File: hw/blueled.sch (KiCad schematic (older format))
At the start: 56 parts, among them J1 Barrel_Jack, J2 LED Strip, J3 ICSP, J4 Screw_Terminal_01x02, Q1 Q_PMOS_SDG, Q2 Q_PNP_EBC, SW2 PUSH, U1 ATmega328P-AU, U2 HC-05, U3 AMS1117-3.3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

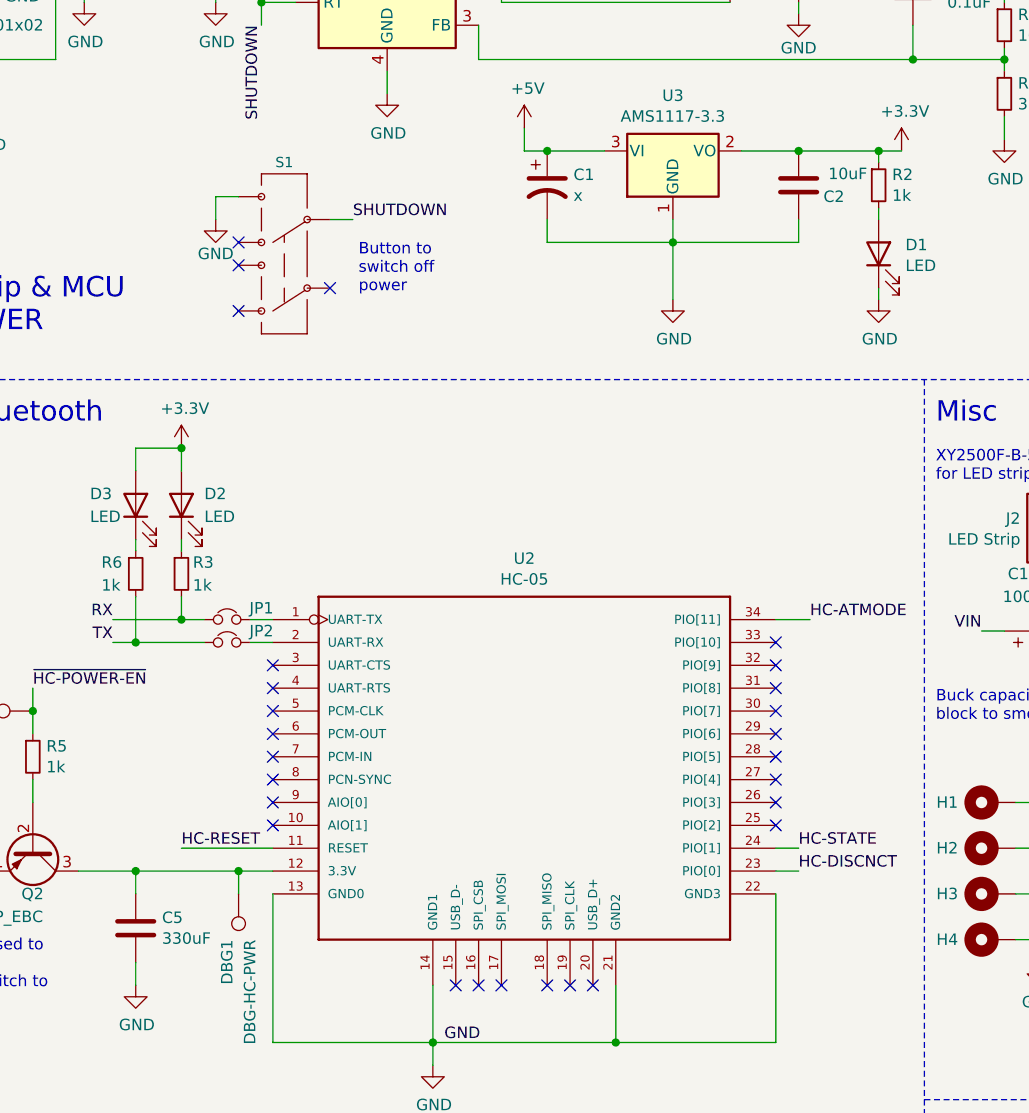
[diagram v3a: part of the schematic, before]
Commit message: add(hw): some capacitors to BOM
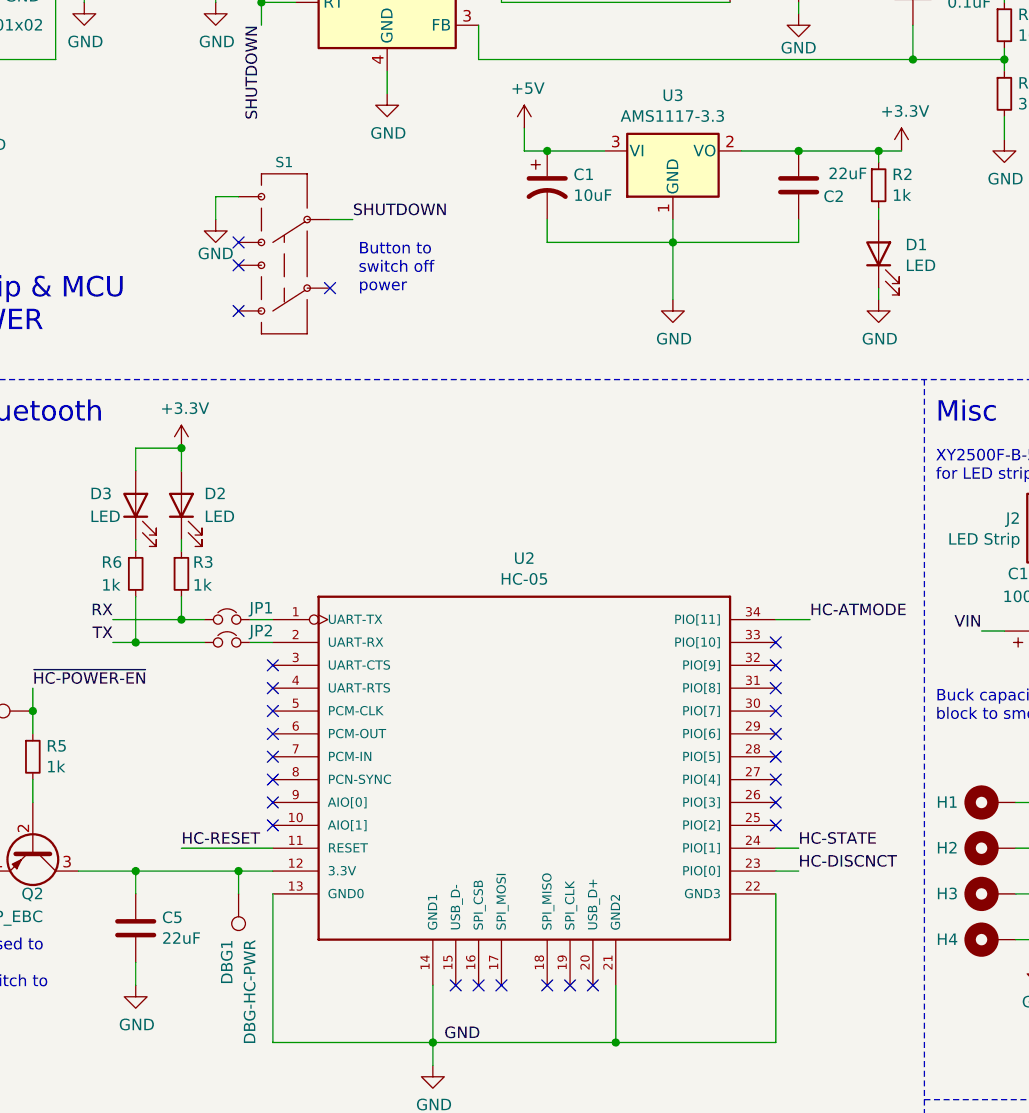
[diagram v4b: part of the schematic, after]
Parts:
- C1: value x -> 10uF
- C12: footprint Capacitor_Tantalum_SMD:CP_EIA-3216-18_Kemet-A_Pad1.58x1.35mm_HandSolder -> Capacitor_SMD:CP_Elec_10x10; Manuf. Part TAJA106K016RNJ -> VEU102M0JTR-1010
- C2: value 10uF -> 22uF; footprint Capacitor_SMD:C_0805_2012Metric_Pad1.15x1.40mm_HandSolder -> Capacitor_Tantalum_SMD:CP_EIA-3216-18_Kemet-A_Pad1.58x1.35mm_HandSolder; Manuf. Part CL21A106MQFNNNE -> 593D226X9004A2TE3
- C5: value 330uF -> 22uF; footprint (none) -> Capacitor_Tantalum_SMD:CP_EIA-3216-18_Kemet-A_Pad1.58x1.35mm_HandSolder; Distributor (none) -> lcsc.com; Manuf. Part (none) -> 593D226X9004A2TE3
- L1: footprint (none) -> blueled:SMMS1350-150M; Manuf. Part SMMS1040-150M -> MWSA1004S-150MT
- R1, R2, R3, R4, R5, R6, R7: Manuf. Part RC0805FR-071KL -> RC0805FR-071KL
- R11: Manuf. Part RK73B2ATTD102J -> RC0805FR-07470RL
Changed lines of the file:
@@
 F 3 "https://datasheet.lcsc.com/szlcsc/1810010118_YAGEO-RC0805FR-071KL_C95781.pdf" H 5100 2300 50  0001 C CNN
 F 4 "lcsc.com" H 5100 2300 50  0001 C CNN "Distributor"
-F 5 " 	RC0805FR-071KL" H 5100 2300 50  0001 C CNN "Manuf. Part"
+F 5 "RC0805FR-071KL" H 5100 2300 50  0001 C CNN "Manuf. Part"
 	1    5100 2300
 	1    0    0    -1
@@
 F 3 "https://datasheet.lcsc.com/szlcsc/1810010118_YAGEO-RC0805FR-071KL_C95781.pdf" H 7800 5050 50  0001 C CNN
 F 4 "lcsc.com" H 7800 5050 50  0001 C CNN "Distributor"
-F 5 " 	RC0805FR-071KL" H 7800 5050 50  0001 C CNN "Manuf. Part"
+F 5 "RC0805FR-071KL" H 7800 5050 50  0001 C CNN "Manuf. Part"
 	1    7800 5050
 	1    0    0    -1
@@
 F 3 "https://datasheet.lcsc.com/szlcsc/1810010118_YAGEO-RC0805FR-071KL_C95781.pdf" H 1850 4000 50  0001 C CNN
 F 4 "lcsc.com" H 1850 4000 50  0001 C CNN "Distributor"
-F 5 " 	RC0805FR-071KL" H 1850 4000 50  0001 C CNN "Manuf. Part"
+F 5 "RC0805FR-071KL" H 1850 4000 50  0001 C CNN "Manuf. Part"
 	1    1850 4000
 	1    0    0    -1
@@
 F 3 "https://datasheet.lcsc.com/szlcsc/1810010118_YAGEO-RC0805FR-071KL_C95781.pdf" H 2050 4000 50  0001 C CNN
 F 4 "lcsc.com" H 2050 4000 50  0001 C CNN "Distributor"
-F 5 " 	RC0805FR-071KL" H 2050 4000 50  0001 C CNN "Manuf. Part"
+F 5 "RC0805FR-071KL" H 2050 4000 50  0001 C CNN "Manuf. Part"
 	1    2050 4000
 	1    0    0    -1
@@
 F 3 "https://datasheet.lcsc.com/szlcsc/1810010118_YAGEO-RC0805FR-071KL_C95781.pdf" H 7700 5050 50  0001 C CNN
 F 4 "lcsc.com" H 7700 5050 50  0001 C CNN "Distributor"
-F 5 " 	RC0805FR-071KL" H 7700 5050 50  0001 C CNN "Manuf. Part"
+F 5 "RC0805FR-071KL" H 7700 5050 50  0001 C CNN "Manuf. Part"
 	1    7700 5050
 	-1   0    0    1
@@
 P 4750 2300
 F 0 "C2" H 4550 2350 50  0000 L CNN
-F 1 "10uF" H 4450 2250 50  0000 L CNN
-F 2 "Capacitor_SMD:C_0805_2012Metric_Pad1.15x1.40mm_HandSolder" H 4788 2150 50  0001 C CNN
-F 3 "https://datasheet.lcsc.com/szlcsc/1810191226_Samsung-Electro-Mechanics-CL21A106MQFNNNE_C41893.pdf" H 4750 2300 50  0001 C CNN
+F 1 "22uF" H 4450 2250 50  0000 L CNN
+F 2 "Capacitor_Tantalum_SMD:CP_EIA-3216-18_Kemet-A_Pad1.58x1.35mm_HandSolder" H 4788 2150 50  0001 C CNN
+F 3 "https://datasheet.lcsc.com/szlcsc/1809131544_Vishay-Intertech-593D226X9004A2TE3_C215881.pdf" H 4750 2300 50  0001 C CNN
 F 4 "lcsc.com" H 4750 2300 50  0001 C CNN "Distributor"
-F 5 "CL21A106MQFNNNE" H 4750 2300 50  0001 C CNN "Manuf. Part"
+F 5 "593D226X9004A2TE3" H 4750 2300 50  0001 C CNN "Manuf. Part"
 	1    4750 2300
 	-1   0    0    1
@@
 F 3 "https://datasheet.lcsc.com/szlcsc/1810010118_YAGEO-RC0805FR-071KL_C95781.pdf" H 9100 2750 50  0001 C CNN
 F 4 "lcsc.com" H 9100 2750 50  0001 C CNN "Distributor"
-F 5 " 	RC0805FR-071KL" H 9100 2750 50  0001 C CNN "Manuf. Part"
+F 5 "RC0805FR-071KL" H 9100 2750 50  0001 C CNN "Manuf. Part"
 	1    9100 2750
 	1    0    0    -1
@@
 P 3650 2300
 F 0 "C1" H 3765 2346 50  0000 L CNN
-F 1 "x" H 3765 2255 50  0000 L CNN
+F 1 "10uF" H 3765 2255 50  0000 L CNN
 F 2 "Capacitor_Tantalum_SMD:CP_EIA-3216-18_Kemet-A_Pad1.58x1.35mm_HandSolder" H 3650 2300 50  0001 C CNN
 F 3 "https://datasheet.lcsc.com/szlcsc/AVX-TAJA106K016RNJ_C7171.pdf" H 3650 2300 50  0001 C CNN
@@
 P 1850 5550
 F 0 "C5" H 1965 5596 50  0000 L CNN
-F 1 "330uF" H 1965 5505 50  0000 L CNN
-F 2 "" H 1888 5400 50  0001 C CNN
-F 3 "" H 1850 5550 50  0001 C CNN
+F 1 "22uF" H 1965 5505 50  0000 L CNN
+F 2 "Capacitor_Tantalum_SMD:CP_EIA-3216-18_Kemet-A_Pad1.58x1.35mm_HandSolder" H 1888 5400 50  0001 C CNN
+F 3 "https://datasheet.lcsc.com/szlcsc/1809131544_Vishay-Intertech-593D226X9004A2TE3_C215881.pdf" H 1850 5550 50  0001 C CNN
+F 4 "593D226X9004A2TE3" H 1850 5550 50  0001 C CNN "Manuf. Part"
+F 5 "lcsc.com" H 1850 5550 50  0001 C CNN "Distributor"
 	1    1850 5550
 	1    0    0    -1
@@
 F 3 "https://datasheet.lcsc.com/szlcsc/1810010118_YAGEO-RC0805FR-071KL_C95781.pdf" H 1400 4800 50  0001 C CNN
 F 4 "lcsc.com" H 1400 4800 50  0001 C CNN "Distributor"
-F 5 " 	RC0805FR-071KL" H 1400 4800 50  0001 C CNN "Manuf. Part"
+F 5 "RC0805FR-071KL" H 1400 4800 50  0001 C CNN "Manuf. Part"
 	1    1400 4800
 	1    0    0    -1
@@
 F 0 "L1" V 5225 1200 50  0000 C CNN
 F 1 "15uH" V 5134 1200 50  0000 C CNN
-F 2 "" H 5000 1200 50  0001 C CNN
-F 3 "https://datasheet.lcsc.com/szlcsc/1809291526_SXN-Shun-Xiang-Nuo-Elec-SMMS1040-150M_C149596.pdf" H 5000 1200 50  0001 C CNN
+F 2 "blueled:SMMS1350-150M" H 5000 1200 50  0001 C CNN
+F 3 "https://datasheet.lcsc.com/szlcsc/1912111437_Sunlord-MWSA1004S-150MT_C408488.pdf" H 5000 1200 50  0001 C CNN
 F 4 "lcsc.com" H 5000 1200 50  0001 C CNN "Distributor"
-F 5 "SMMS1040-150M" H 5000 1200 50  0001 C CNN "Manuf. Part"
+F 5 "MWSA1004S-150MT" H 5000 1200 50  0001 C CNN "Manuf. Part"
 	1    5000 1200
 	0    -1   -1   0
@@
 F 1 "470" V 8850 3800 50  0000 L CNN
 F 2 "Resistor_SMD:R_0805_2012Metric_Pad1.15x1.40mm_HandSolder" H 9050 3850 50  0001 C CNN
-F 3 "https://datasheet.lcsc.com/szlcsc/1810301711_KOA-Speer-Elec-RK73B2ATTD102J_C159911.pdf" H 9050 3850 50  0001 C CNN
+F 3 "https://datasheet.lcsc.com/szlcsc/1810311431_YAGEO-RC0805FR-07470RL_C114564.pdf" H 9050 3850 50  0001 C CNN
 F 4 "lcsc.com" H 9050 3850 50  0001 C CNN "Distributor"
-F 5 "RK73B2ATTD102J" H 9050 3850 50  0001 C CNN "Manuf. Part"
+F 5 "RC0805FR-07470RL" H 9050 3850 50  0001 C CNN "Manuf. Part"
 	1    9050 3850
 	0    -1   -1   0
@@
 F 0 "C12" V 6050 4250 50  0000 L CNN
 F 1 "1000uF" V 5950 4150 50  0000 L CNN
-F 2 "Capacitor_Tantalum_SMD:CP_EIA-3216-18_Kemet-A_Pad1.58x1.35mm_HandSolder" H 5800 4250 50  0001 C CNN
-F 3 "https://datasheet.lcsc.com/szlcsc/AVX-TAJA106K016RNJ_C7171.pdf" H 5800 4250 50  0001 C CNN
+F 2 "Capacitor_SMD:CP_Elec_10x10" H 5800 4250 50  0001 C CNN
+F 3 "https://datasheet.lcsc.com/szlcsc/1912111437_Lelon-VEU102M0JTR-1010_C249735.pdf" H 5800 4250 50  0001 C CNN
 F 4 "lcsc.com" H 5800 4250 50  0001 C CNN "Distributor"
-F 5 "TAJA106K016RNJ" H 5800 4250 50  0001 C CNN "Manuf. Part"
+F 5 "VEU102M0JTR-1010" H 5800 4250 50  0001 C CNN "Manuf. Part"
 	1    5800 4250
 	0    -1   -1   0

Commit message: add(hw): almost done with assigning capacitors
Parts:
- C10: footprint (none) -> Capacitor_SMD:C_1206_3216Metric_Pad1.42x1.75mm_HandSolder; Manuf. Part (none) -> GRM31CR60J107ME39L
- C11: footprint Capacitor_SMD:C_0603_1608Metric_Pad1.05x0.95mm_HandSolder -> Capacitor_SMD:C_0805_2012Metric_Pad1.15x1.40mm_HandSolder; Manuf. Part CC0402KRX7R0BB102 -> C2012X7R2A102KT020S
- C6: footprint Capacitor_SMD:C_1210_3225Metric_Pad1.42x2.65mm_HandSolder -> Capacitor_SMD:C_1206_3216Metric_Pad1.42x1.75mm_HandSolder; Manuf. Part C3225X7S2A475KT000N -> CGA5L3X7S2A225KT0Y0N
- C7: Manuf. Part CC0805KKX7R9BB684 -> C2012X7S2A684KT000N
- C8: footprint (none) -> Capacitor_SMD:C_0805_2012Metric_Pad1.15x1.40mm_HandSolder; Manuf. Part (none) -> C2012X7R1C474KT000N
- C9: footprint (none) -> Capacitor_SMD:C_0805_2012Metric_Pad1.15x1.40mm_HandSolder; Manuf. Part (none) -> C2012C0G1H472JT0H0N
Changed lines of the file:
@@
 F 0 "C9" H 5400 1500 50  0000 L CNN
 F 1 "0.1uF" H 5400 1400 50  0000 L CNN
-F 2 "" H 5288 1300 50  0001 C CNN
-F 3 "" H 5250 1450 50  0001 C CNN
+F 2 "Capacitor_SMD:C_0805_2012Metric_Pad1.15x1.40mm_HandSolder" H 5288 1300 50  0001 C CNN
+F 3 "https://datasheet.lcsc.com/szlcsc/1912111437_TDK-C2012C0G1H472JT0H0N_C342964.pdf" H 5250 1450 50  0001 C CNN
 F 4 "lcsc.com" H 5250 1450 50  0001 C CNN "Distributor"
-F 5 "" H 5250 1450 50  0001 C CNN "Manuf. Part"
+F 5 "C2012C0G1H472JT0H0N" H 5250 1450 50  0001 C CNN "Manuf. Part"
 	1    5250 1450
 	1    0    0    -1
@@
 F 0 "C10" H 6115 1771 50  0000 L CNN
 F 1 "100uF" H 6115 1680 50  0000 L CNN
-F 2 "" H 6000 1725 50  0001 C CNN
-F 3 "" H 6000 1725 50  0001 C CNN
+F 2 "Capacitor_SMD:C_1206_3216Metric_Pad1.42x1.75mm_HandSolder" H 6000 1725 50  0001 C CNN
+F 3 "https://datasheet.lcsc.com/szlcsc/1810201321_Murata-Electronics-GRM31CR60J107ME39L_C77085.pdf" H 6000 1725 50  0001 C CNN
 F 4 "lcsc.com" H 6000 1725 50  0001 C CNN "Distributor"
-F 5 "" H 6000 1725 50  0001 C CNN "Manuf. Part"
+F 5 "GRM31CR60J107ME39L" H 6000 1725 50  0001 C CNN "Manuf. Part"
 	1    6000 1725
 	1    0    0    -1
@@
 F 0 "C6" H 1725 1300 50  0000 L CNN
 F 1 "4.7uF" H 1675 1150 50  0000 L CNN
-F 2 "Capacitor_SMD:C_1210_3225Metric_Pad1.42x2.65mm_HandSolder" H 1625 1250 50  0001 C CNN
-F 3 "https://datasheet.lcsc.com/szlcsc/1912111437_TDK-C3225X7S2A475KT000N_C342614.pdf" H 1625 1250 50  0001 C CNN
+F 2 "Capacitor_SMD:C_1206_3216Metric_Pad1.42x1.75mm_HandSolder" H 1625 1250 50  0001 C CNN
+F 3 "https://datasheet.lcsc.com/szlcsc/1912111437_TDK-CGA5L3X7S2A225KT0Y0N_C342669.pdf" H 1625 1250 50  0001 C CNN
 F 4 "lcsc.com" H 1625 1250 50  0001 C CNN "Distributor"
-F 5 "C3225X7S2A475KT000N" H 1625 1250 50  0001 C CNN "Manuf. Part"
+F 5 "CGA5L3X7S2A225KT0Y0N" H 1625 1250 50  0001 C CNN "Manuf. Part"
 	1    1625 1250
 	1    0    0    -1
@@
 F 0 "C11" H 3350 1050 50  0000 L CNN
 F 1 "1nF" H 3350 1150 50  0000 L CNN
-F 2 "Capacitor_SMD:C_0603_1608Metric_Pad1.05x0.95mm_HandSolder" H 3638 900 50  0001 C CNN
-F 3 "https://datasheet.lcsc.com/szlcsc/2005222139_YAGEO-CC0402KRX7R0BB102_C527013.pdf" H 3600 1050 50  0001 C CNN
+F 2 "Capacitor_SMD:C_0805_2012Metric_Pad1.15x1.40mm_HandSolder" H 3638 900 50  0001 C CNN
+F 3 "https://datasheet.lcsc.com/szlcsc/1912111437_TDK-C2012X7R2A102KT020S_C415298.pdf" H 3600 1050 50  0001 C CNN
 F 4 "lcsc.com" H 3600 1050 50  0001 C CNN "Distributor"
-F 5 "CC0402KRX7R0BB102" H 3600 1050 50  0001 C CNN "Manuf. Part"
+F 5 "C2012X7R2A102KT020S" H 3600 1050 50  0001 C CNN "Manuf. Part"
 	1    3600 1050
 	0    1    1    0
@@
 F 0 "C8" H 3325 1050 50  0000 L CNN
 F 1 "0.47uF" H 3475 1050 50  0000 L CNN
-F 2 "" H 3450 850 50  0001 C CNN
-F 3 "" H 3450 850 50  0001 C CNN
+F 2 "Capacitor_SMD:C_0805_2012Metric_Pad1.15x1.40mm_HandSolder" H 3450 850 50  0001 C CNN
+F 3 "https://datasheet.lcsc.com/szlcsc/2009111606_TDK-C2012X7R1C474KT000N_C694187.pdf" H 3450 850 50  0001 C CNN
 F 4 "lcsc.com" H 3450 850 50  0001 C CNN "Distributor"
-F 5 "" H 3450 850 50  0001 C CNN "Manuf. Part"
+F 5 "C2012X7R1C474KT000N" H 3450 850 50  0001 C CNN "Manuf. Part"
 	1    3450 850
 	1    0    0    -1
@@
 F 1 "680nF" H 1950 1150 50  0000 L CNN
 F 2 "Capacitor_SMD:C_0805_2012Metric_Pad1.15x1.40mm_HandSolder" H 2238 1100 50  0001 C CNN
-F 3 "https://datasheet.lcsc.com/szlcsc/1810311413_YAGEO-CC0805KKX7R9BB684_C107133.pdf" H 2200 1250 50  0001 C CNN
+F 3 "https://datasheet.lcsc.com/szlcsc/2004221632_TDK-C2012X7S2A684KT000N_C516764.pdf" H 2200 1250 50  0001 C CNN
 F 4 "lcsc.com" H 2200 1250 50  0001 C CNN "Distributor"
-F 5 "CC0805KKX7R9BB684" H 2200 1250 50  0001 C CNN "Manuf. Part"
+F 5 "C2012X7S2A684KT000N" H 2200 1250 50  0001 C CNN "Manuf. Part"
 	1    2200 1250
 	1    0    0    -1

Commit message: add(hw): update resistors in BOM
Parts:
- R10, R14: footprint Resistor_SMD:R_0603_1608Metric_Pad1.05x0.95mm_HandSolder -> Resistor_SMD:R_0805_2012Metric_Pad1.15x1.40mm_HandSolder
- R12: footprint Resistor_SMD:R_0603_1608Metric_Pad1.05x0.95mm_HandSolder -> Resistor_SMD:R_0805_2012Metric_Pad1.15x1.40mm_HandSolder; Manuf. Part RC0603FR-072K1L -> RC0805FR-072K1L
- R9: footprint Resistor_SMD:R_0603_1608Metric_Pad1.05x0.95mm_HandSolder -> Resistor_SMD:R_0805_2012Metric_Pad1.15x1.40mm_HandSolder; Manuf. Part MCR03ERTF3401 -> RC0805FR-073K4L
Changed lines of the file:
@@
 F 0 "R9" H 5709 1946 50  0000 L CNN
 F 1 "3.4k" H 5709 1855 50  0000 L CNN
-F 2 "Resistor_SMD:R_0603_1608Metric_Pad1.05x0.95mm_HandSolder" H 5650 1900 50  0001 C CNN
-F 3 "https://datasheet.lcsc.com/szlcsc/ROHM-Semicon-MCR03ERTF3401_C308067.pdf" H 5650 1900 50  0001 C CNN
+F 2 "Resistor_SMD:R_0805_2012Metric_Pad1.15x1.40mm_HandSolder" H 5650 1900 50  0001 C CNN
+F 3 "https://datasheet.lcsc.com/szlcsc/YAGEO-AC0805FR-073K4L_C228795.pdf" H 5650 1900 50  0001 C CNN
 F 4 "lcsc.com" H 5650 1900 50  0001 C CNN "Distributor"
-F 5 "MCR03ERTF3401" H 5650 1900 50  0001 C CNN "Manuf. Part"
+F 5 "RC0805FR-073K4L " H 5650 1900 50  0001 C CNN "Manuf. Part"
 	1    5650 1900
 	1    0    0    -1
@@
 F 0 "R12" V 3600 1125 50  0000 L CNN
 F 1 "2.1k" V 3500 1125 50  0000 L CNN
-F 2 "Resistor_SMD:R_0603_1608Metric_Pad1.05x0.95mm_HandSolder" V 3530 1200 50  0001 C CNN
-F 3 "https://datasheet.lcsc.com/szlcsc/1811082014_YAGEO-RC0603FR-072K1L_C245950.pdf" H 3600 1200 50  0001 C CNN
+F 2 "Resistor_SMD:R_0805_2012Metric_Pad1.15x1.40mm_HandSolder" V 3530 1200 50  0001 C CNN
+F 3 "https://datasheet.lcsc.com/szlcsc/2001062136_YAGEO-RC0805FR-072K1L_C273922.pdf" H 3600 1200 50  0001 C CNN
 F 4 "lcsc.com" H 3600 1200 50  0001 C CNN "Distributor"
-F 5 "RC0603FR-072K1L" H 3600 1200 50  0001 C CNN "Manuf. Part"
+F 5 "RC0805FR-072K1L" H 3600 1200 50  0001 C CNN "Manuf. Part"
 	1    3600 1200
 	0    -1   -1   0
@@
 F 0 "R10" H 5709 1646 50  0000 L CNN
 F 1 "10k" H 5709 1555 50  0000 L CNN
-F 2 "Resistor_SMD:R_0603_1608Metric_Pad1.05x0.95mm_HandSolder" H 5650 1600 50  0001 C CNN
+F 2 "Resistor_SMD:R_0805_2012Metric_Pad1.15x1.40mm_HandSolder" H 5650 1600 50  0001 C CNN
 F 3 "https://datasheet.lcsc.com/szlcsc/1810201611_YAGEO-RC0805FR-0710KL_C84376.pdf" H 5650 1600 50  0001 C CNN
 F 4 "lcsc.com" H 5650 1600 50  0001 C CNN "Distributor"
@@
 F 0 "R14" H 6059 1446 50  0000 L CNN
 F 1 "10k" H 6059 1355 50  0000 L CNN
-F 2 "Resistor_SMD:R_0603_1608Metric_Pad1.05x0.95mm_HandSolder" H 6000 1400 50  0001 C CNN
+F 2 "Resistor_SMD:R_0805_2012Metric_Pad1.15x1.40mm_HandSolder" H 6000 1400 50  0001 C CNN
 F 3 "https://datasheet.lcsc.com/szlcsc/1810201611_YAGEO-RC0805FR-0710KL_C84376.pdf" H 6000 1400 50  0001 C CNN
 F 4 "lcsc.com" H 6000 1400 50  0001 C CNN "Distributor"
